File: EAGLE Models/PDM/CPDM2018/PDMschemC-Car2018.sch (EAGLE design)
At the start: 13 parts, among them K1 35701331, K2 35701331, K3 35701331

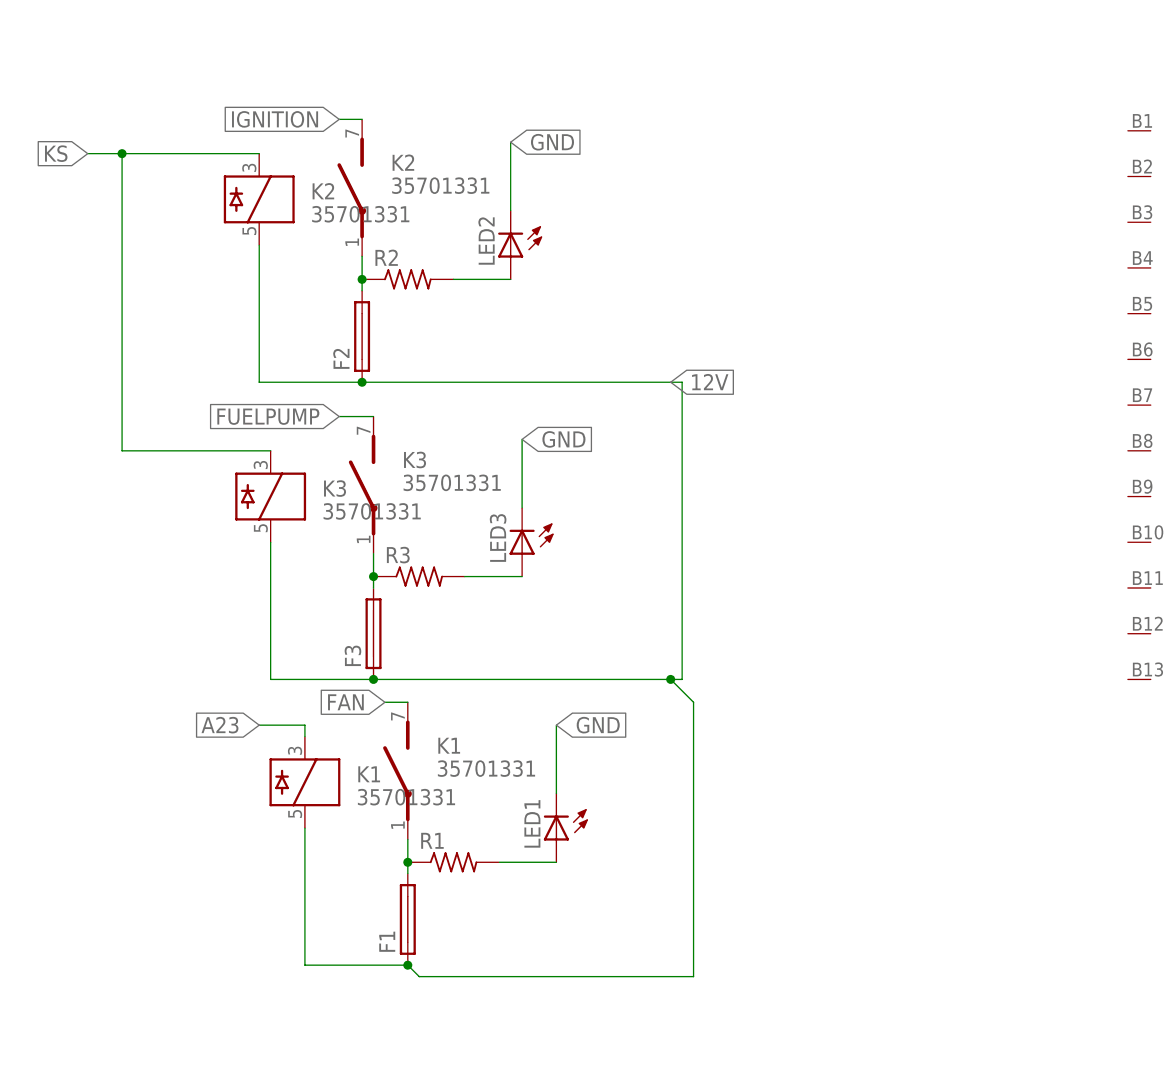
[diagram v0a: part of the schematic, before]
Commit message: Replaced parts in schematic
Most of the parts used in the first iteration of the schematic did not have the right package so they were replaced by parts taht did.
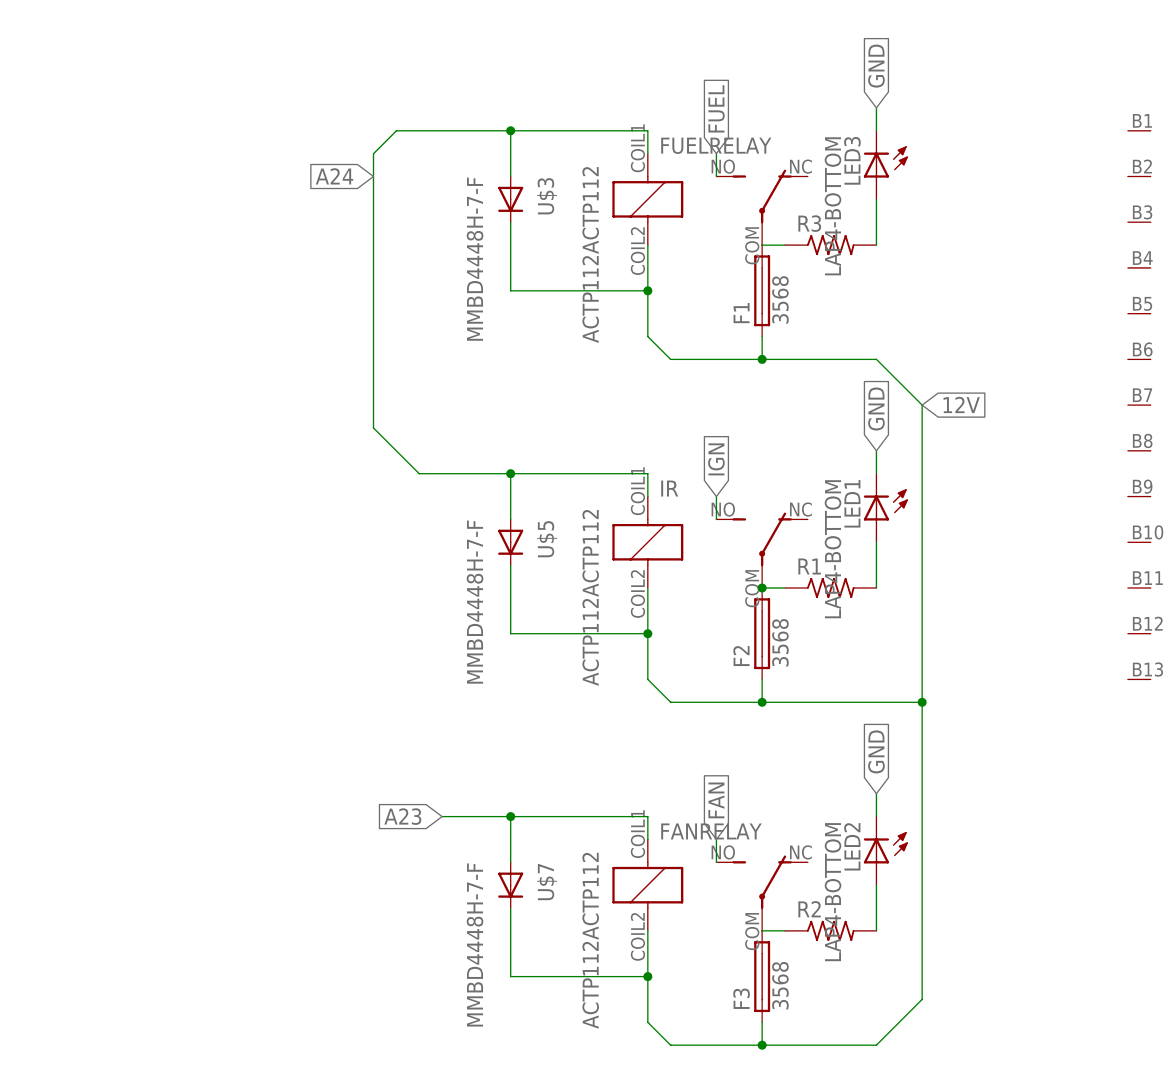
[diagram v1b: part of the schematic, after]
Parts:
- removed K1, K2, K3: 35701331, relay:35701331
- added FANRELAY, FUELRELAY, IR: ACTP112ACTP112, panasonic:ACTP112ACTP112
- added U$3, U$5, U$7: MMBD4448H-7-F, diodes-inc:MMBD4448H-7-F
- F1, F2, F3: value (none) -> 3568; device fuse:GSH15 -> Keystone:3568
- LED1, LED2, LED3: value (none) -> LAP4-BOTTOM; device led:LED -> led:LAP4-BOTTOM
- R1, R2, R3: device resistor:R-US_0204/2V -> resistor:R-US_R1206
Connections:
- removed net FUELPUMP: K32.S
- removed net IGNITION: K22.S
- removed net KS: K21.3, K31.3
- removed net N$1 (its old number): F1.2, K12.P, R1.1
- removed net N$8: F3.2, K32.P, R3.1
- new net A24: FUELRELAY.COIL1, IR.COIL1, U$3.A, U$5.A
- new net FUEL: FUELRELAY.NO
- new net IGN: IR.NO
- new net N$2: R2.1
- new net N$3: F1.2, FUELRELAY.COM
- new net N$6: F2.2, IR.COM, R1.1
- new net N$9: F3.2, FANRELAY.COM
- net 12V: now also FANRELAY.COIL2, FUELRELAY.COIL2, IR.COIL2, U$3.C, U$5.C, U$7.C; no longer K11.5, K21.5, K31.5
- net A23: now also FANRELAY.COIL1, U$7.A; no longer K11.3
- net FAN: now also FANRELAY.NO; no longer K12.S
- net N$5: now also R3.1; no longer F2.2, K22.P, R2.1
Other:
- moved on the sheet: LED1, LED2, LED3, R1, R2, R3

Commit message: Connected pins
Connected two pins on output
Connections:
- new net N$8: U$1.B12, U$1.B13
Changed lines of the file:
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@@
+</segment>
+</net>
+<net name="N$8" class="0">
+<segment>
+<pinref part="U$1" gate="G$1" pin="B13"/>
+<wire x1="205.74" y1="73.66" x2="208.28" y2="73.66" width="0.1524" layer="91"/>
+<wire x1="208.28" y1="73.66" x2="208.28" y2="78.74" width="0.1524" layer="91"/>
+<pinref part="U$1" gate="G$1" pin="B12"/>
+<wire x1="208.28" y1="78.74" x2="205.74" y2="78.74" width="0.1524" layer="91"/>
+<label x="208.28" y="76.2" size="1.778" layer="95" xref="yes"/>
 </segment>
 </net>

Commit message: C-Car PDM
Assigned Pin Connections
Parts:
- added F4, F5, F6: 3568, Keystone:3568
- added LED4, LED5, LED6: LAP4-BOTTOM, led:LAP4-BOTTOM
- added R4, R5, R6: (no value), resistor:R-US_R1206
- added U$2: STPS20L15G-TRTO, st-microelectronics:STPS20L15G-TRTO
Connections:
- removed net A23: FANRELAY.COIL1, U$7.A
- removed net A24: FUELRELAY.COIL1, IR.COIL1, U$3.A, U$5.A
- new net B23: FANRELAY.COIL1, U$1.B6, U$7.A
- new net DAQ: F5.1, R5.1, U$1.B1, U$1.B2
- new net ECU: F4.1, R6.1, U$1.B14, U$1.B8, U$2.K, U$2.P1
- new net KILLSWITCH: FUELRELAY.COIL1, IR.COIL1, U$1.B7, U$3.A, U$5.A
- new net N$10: LED5.A, R5.2
- new net N$11: LED6.A, R6.2
- new net N$17: U$1.B5
- new net SH/B: F6.1, R4.1, U$1.B20, U$1.B21
- net 12V: now also F4.2, F5.2, F6.2, U$1.B3, U$1.B4
- net FAN: now also U$1.B26
- net FUEL: now also U$1.B19
- net GND: now also LED4.C, LED5.C, LED6.C, U$1.B10, U$1.B11, U$1.B12, U$1.B15, U$1.B16, U$1.B17, U$1.B18, U$1.B22, U$1.B23, U$1.B24, U$1.B25, U$1.B9
- net IGN: now also U$1.B13
- net N$8: now also LED4.A, R4.2; no longer U$1.B12, U$1.B13

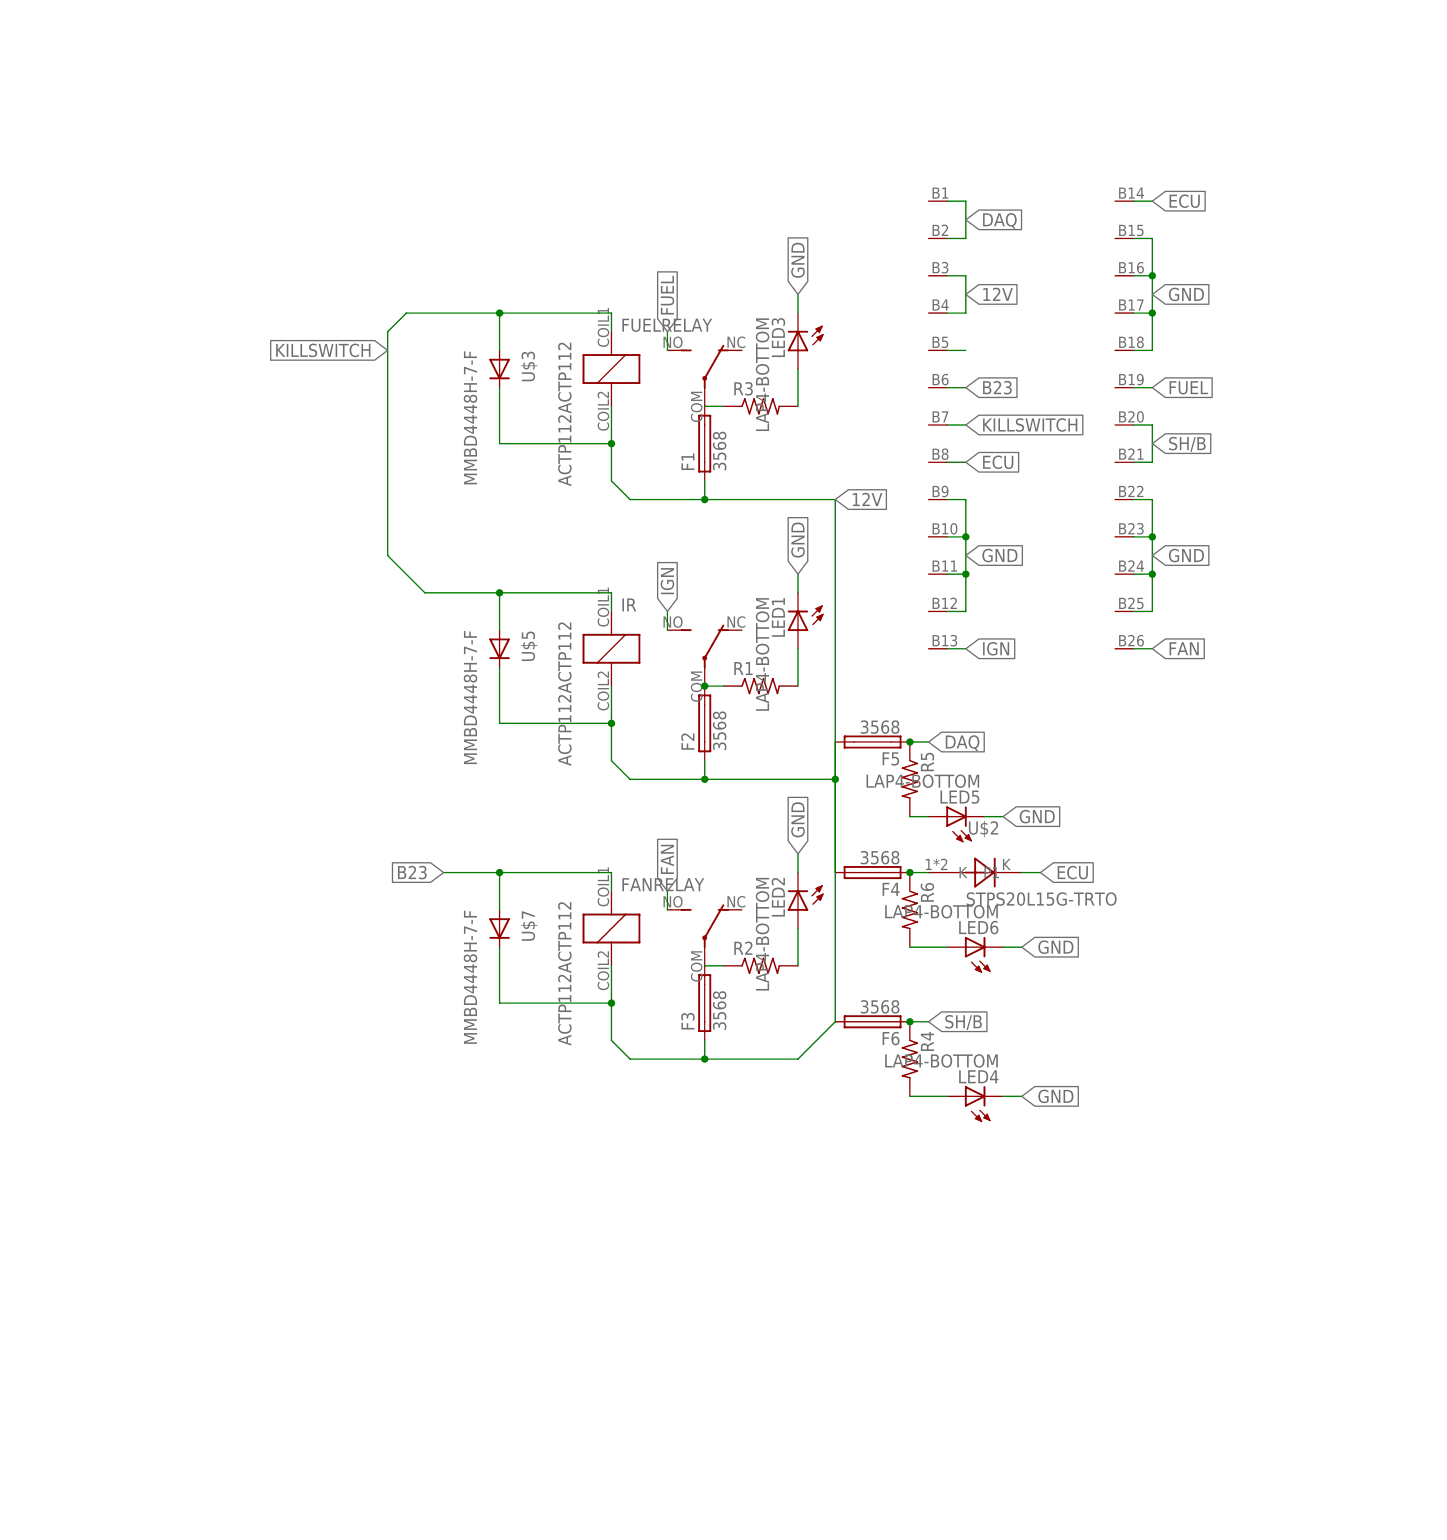
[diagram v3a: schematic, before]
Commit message: Cleaned up schematic
Grouped connections and replaced some traces with labels to improve readability.
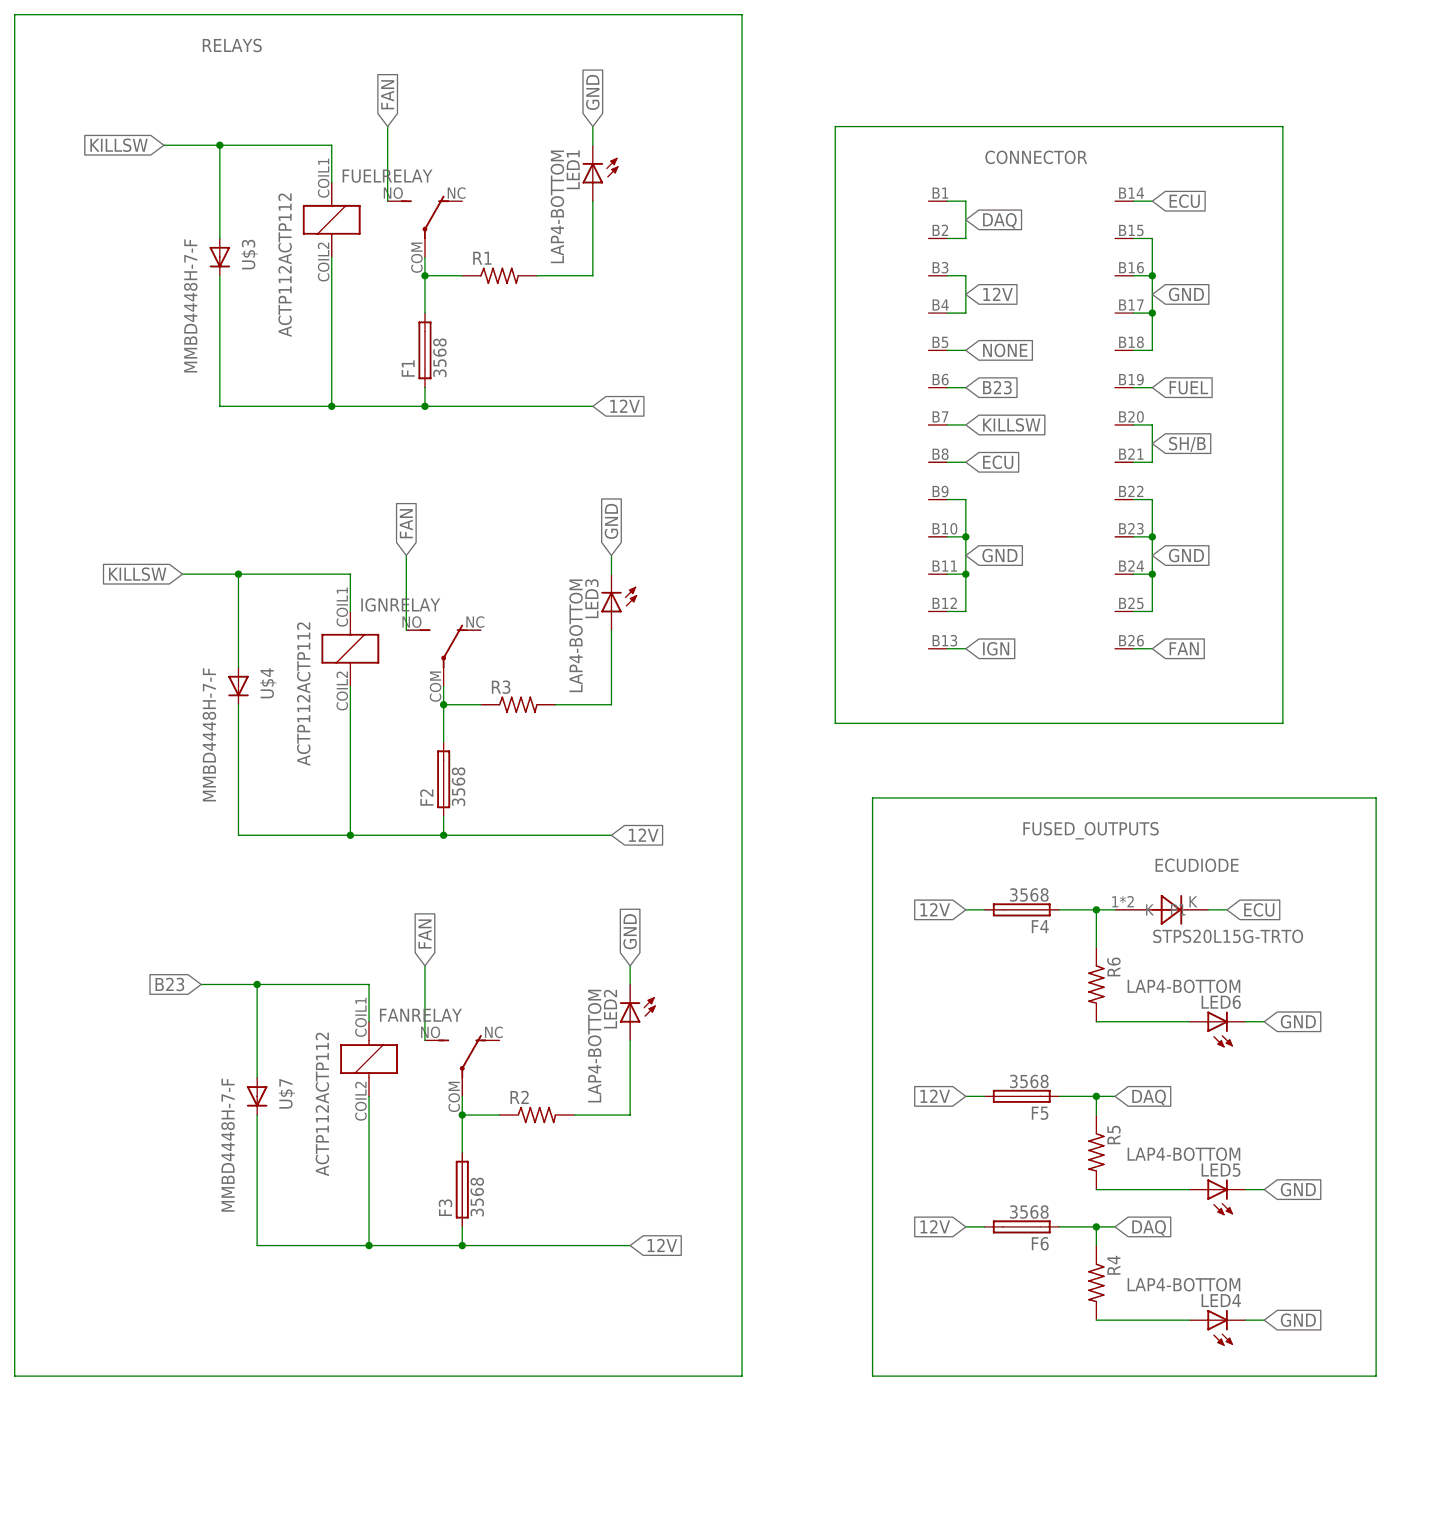
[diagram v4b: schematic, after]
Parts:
- removed IR: ACTP112ACTP112, panasonic:ACTP112ACTP112
- removed U$2: STPS20L15G-TRTO, st-microelectronics:STPS20L15G-TRTO
- removed U$5: MMBD4448H-7-F, diodes-inc:MMBD4448H-7-F
- added ECUDIODE: STPS20L15G-TRTO, st-microelectronics:STPS20L15G-TRTO
- added IGNRELAY: ACTP112ACTP112, panasonic:ACTP112ACTP112
- added U$4: MMBD4448H-7-F, diodes-inc:MMBD4448H-7-F
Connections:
- net N$17 renamed NONE
- removed net KILLSWITCH: FUELRELAY.COIL1, IR.COIL1, U$1.B7, U$3.A, U$5.A
- removed net N$2 (its old number): R2.1
- removed net N$5 (its old number): R3.1
- new net KILLSW: FUELRELAY.COIL1, IGNRELAY.COIL1, U$1.B7, U$3.A, U$4.A
- new net N$1: F3.2, FANRELAY.COM, R2.1
- net 12V: now also IGNRELAY.COIL2, U$4.C; no longer IR.COIL2, U$5.C
- net DAQ: now also F6.1, R4.1
- net ECU: now also ECUDIODE.K; no longer F4.1, R6.1, U$2.K, U$2.P1
- net FAN: now also FUELRELAY.NO, IGNRELAY.NO
- net FUEL: no longer FUELRELAY.NO
- net IGN: no longer IR.NO
- net N$3: now also R1.1
- net N$6: now also IGNRELAY.COM, R3.1; no longer IR.COM, R1.1
- net N$9: now also ECUDIODE.P1, F4.1, R6.1; no longer F3.2, FANRELAY.COM
- net SH/B: no longer F6.1, R4.1
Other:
- moved on the sheet: F1, F2, F3, F4, F5, F6, FANRELAY, FUELRELAY, LED1, LED2, LED3, LED4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

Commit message: Began PDM board design
Placed components on the board. Waiting on current draw tests to determine trace widths.
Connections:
- removed net B23: FANRELAY.COIL1, U$1.B6, U$7.A
- removed net NONE: U$1.B5
- new net A23: FANRELAY.COIL1, U$1.B7, U$7.A
- net 12V: now also ECUDIODE.P1, U$1.B5; no longer F4.2, U$1.B3
- net DAQ: no longer F6.1, R4.1
- net ECU: now also F4.1, R6.1, U$1.B20, U$1.B21; no longer ECUDIODE.K, U$1.B14, U$1.B8
- net FAN: no longer FUELRELAY.NO, IGNRELAY.NO
- net FUEL: now also FUELRELAY.NO
- net IGN: now also IGNRELAY.NO
- net KILLSW: now also U$1.B6; no longer U$1.B7
- net N$9: now also ECUDIODE.K, F4.2; no longer ECUDIODE.P1, F4.1, R6.1
- net SH/B: now also F6.1, R4.1, U$1.B14, U$1.B8; no longer U$1.B20, U$1.B21
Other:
- moved on the sheet: ECUDIODE, F4, LED6, R6
